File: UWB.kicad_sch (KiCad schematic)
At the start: 9 parts, among them U1 DWM3000TR13

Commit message: Final Routing
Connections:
- net +3.3V renamed +3.3V_Sensors
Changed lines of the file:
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@@
+	)
+	(junction
+		(at 177.8 90.17)
+		(diameter 0)
+		(color 0 0 0 0)
+	)
+	(junction
+		(at 111.76 87.63)
+		(diameter 0)
+		(color 0 0 0 0)
 	)
 	(junction
@@
 	)
 	(junction
-		(at 177.8 90.17)
-		(diameter 0)
-		(color 0 0 0 0)
-	)
-	(junction
-		(at 111.76 87.63)
-		(diameter 0)
-		(color 0 0 0 0)
-	)
-	(junction
 		(at 168.91 80.01)
 		(diameter 0)
@@
 		(pts
 			(xy 125.73 92.71) (xy 111.76 92.71)
+		)
+		(stroke
+			(width 0)
+			(type default)
+		)
+	)
+	(wire
+		(pts
+			(xy 101.6 78.74) (xy 101.6 87.63)
 		)
 		(stroke
@@
 			)
 			(justify right)
+		)
+	)
+	(hierarchical_label "+3.3V_Sensors"
+		(shape input)
+		(at 101.6 78.74 90)
+		(effects
+			(font
+				(size 1.27 1.27)
+			)
+			(justify left)
 		)
 	)
@@
 					(unit 1)
 				)
-			)
-		)
-	)
-	(symbol
-		(lib_id "power:+3.3V")
-		(at 101.6 87.63 0)
-		(unit 1)
-		(body_style 1)
-		(exclude_from_sim no)
-		(in_bom yes)
-		(on_board yes)
-		(in_pos_files yes)
-		(dnp no)
-		(fields_autoplaced yes)
-		(property "Reference" "#PWR02"
-			(at 101.6 91.44 0)
-			(hide yes)
-			(show_name no)
-			(do_not_autoplace no)
-			(effects
-				(font
-					(size 1.27 1.27)
-				)
-			)
-		)
-		(property "Value" "+3.3V"
-			(at 101.6 82.55 0)
-			(show_name no)
-			(do_not_autoplace no)
-			(effects
-				(font
-					(size 1.27 1.27)
-				)
-			)
-		)
-		(property "Footprint" "Package_SO:TSSOP-20_4.4x6.5mm_P0.65mm"
-			(at 101.6 87.63 0)
-			(hide yes)
-			(show_name no)
-			(do_not_autoplace no)
-			(effects
-				(font
-					(size 1.27 1.27)
-				)
-			)
-		)
-		(property "Datasheet" ""
-			(at 101.6 87.63 0)
-			(hide yes)
-			(show_name no)
-			(do_not_autoplace no)
-			(effects
-				(font
-					(size 1.27 1.27)
-				)
-			)
-		)
-		(property "Description" "Power symbol creates a global label with name \"+3.3V\""
-			(at 101.6 87.63 0)
-			(hide yes)
-			(show_name no)
-			(do_not_autoplace no)
-			(effects
-				(font
-					(size 1.27 1.27)
-				)
-			)
-		)
-		(pin "1"
-		)
-		(instances
-			(project "SuperNicePCB"
-				(path "/794e52b0-48ac-4476-a221-597be743d898/f7354725-387d-4beb-b227-ebab880fa3d1"
-					(reference "#PWR02")
-					(unit 1)
-				)

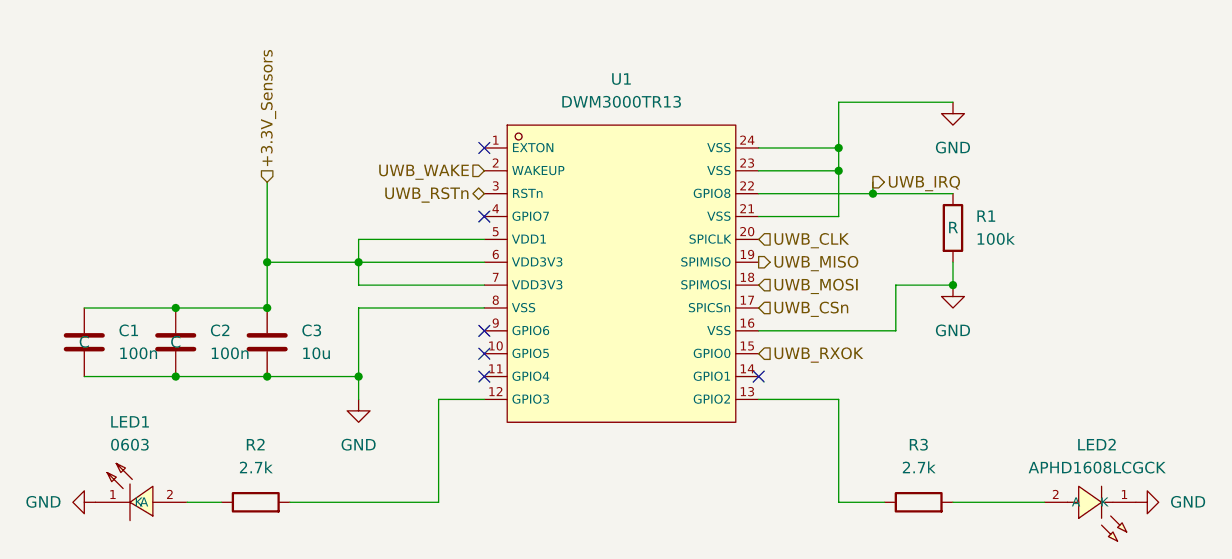
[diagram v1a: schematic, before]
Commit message: UWB: add test points
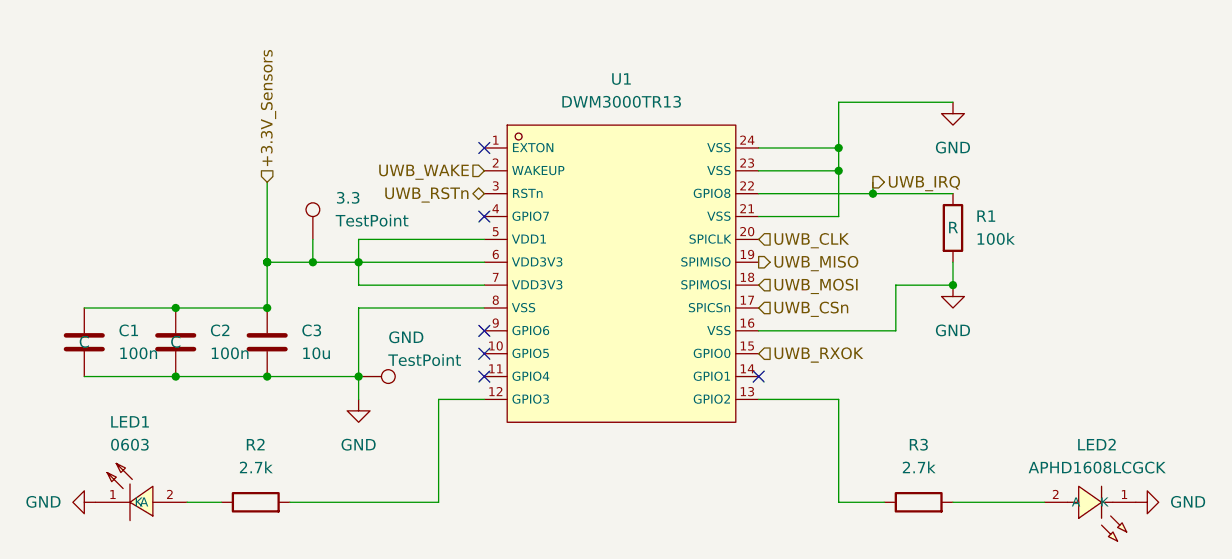
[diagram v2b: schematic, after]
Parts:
- added 3.3: TestPoint, Package_TO_SOT_SMD:SOT-23-5, symbol Connector:TestPoint
- added GND: TestPoint, symbol Connector:TestPoint
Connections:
- net +3.3V_Sensors: now also 3.3.1
- net GND: now also GND.1
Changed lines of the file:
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@@
+	)
+	(junction
+		(at 101.6 87.63)
+		(diameter 0)
+		(color 0 0 0 0)
+	)
+	(junction
+		(at 106.68 87.63)
+		(diameter 0)
+		(color 0 0 0 0)
 	)
 	(junction
@@
 	(wire
 		(pts
+			(xy 106.68 87.63) (xy 111.76 87.63)
+		)
+		(stroke
+			(width 0)
+			(type default)
+		)
+	)
+	(wire
+		(pts
 			(xy 165.1 77.47) (xy 165.1 82.55)
 		)
@@
 	(wire
 		(pts
-			(xy 101.6 87.63) (xy 111.76 87.63)
+			(xy 101.6 87.63) (xy 106.68 87.63)
 		)
 		(stroke
@@
 		(pts
 			(xy 171.45 95.25) (xy 171.45 90.17)
+		)
+		(stroke
+			(width 0)
+			(type default)
+		)
+	)
+	(wire
+		(pts
+			(xy 106.68 85.09) (xy 106.68 87.63)
 		)
 		(stroke
@@
 					(unit 1)
 				)
+			)
+		)
+	)
+	(symbol
+		(lib_id "Connector:TestPoint")
+		(at 111.76 100.33 270)
+		(unit 1)
+		(body_style 1)
+		(exclude_from_sim no)
+		(in_bom yes)
+		(on_board yes)
+		(in_pos_files yes)
+		(dnp no)
+		(property "Reference" "GND"
+			(at 115.062 96.012 90)
+			(show_name no)
+			(do_not_autoplace no)
+			(effects
+				(font
+					(size 1.27 1.27)
+				)
+				(justify left)
+			)
+		)
+		(property "Value" "TestPoint"
+			(at 115.062 98.552 90)
+			(show_name no)
+			(do_not_autoplace no)
+			(effects
+				(font
+					(size 1.27 1.27)
+				)
+				(justify left)
+			)
+		)
+		(property "Footprint" ""
+			(at 111.76 105.41 0)
+			(hide yes)
+			(show_name no)
+			(do_not_autoplace no)
+			(effects
+				(font
+					(size 1.27 1.27)
+				)
+			)
+		)
+		(property "Datasheet" ""
+			(at 111.76 105.41 0)
+			(hide yes)
+			(show_name no)
+			(do_not_autoplace no)
+			(effects
+				(font
+					(size 1.27 1.27)
+				)
+			)
+		)
+		(property "Description" "test point"
+			(at 111.76 100.33 0)
+			(hide yes)
+			(show_name no)
+			(do_not_autoplace no)
+			(effects
+				(font
+					(size 1.27 1.27)
+				)
+			)
+		)
+		(pin "1"
+		)
+		(instances
+			(project "SuperNicePCB"
+				(path "/794e52b0-48ac-4476-a221-597be743d898/f7354725-387d-4beb-b227-ebab880fa3d1"
+					(reference "GND")
+					(unit 1)
+				)
+			)
+		)
+	)
+	(symbol
+		(lib_id "Connector:TestPoint")
+		(at 106.68 85.09 0)
+		(unit 1)
+		(body_style 1)
+		(exclude_from_sim no)
+		(in_bom yes)
+		(on_board yes)
+		(in_pos_files yes)
+		(dnp no)
+		(fields_autoplaced yes)
+		(property "Reference" "3.3"
+			(at 109.22 80.5179 0)
+			(show_name no)
+			(do_not_autoplace no)
+			(effects
+				(font
+					(size 1.27 1.27)
+				)
+				(justify left)
+			)
+		)
+		(property "Value" "TestPoint"
+			(at 109.22 83.0579 0)
+			(show_name no)
+			(do_not_autoplace no)
+			(effects
+				(font
+					(size 1.27 1.27)
+				)
+				(justify left)
+			)
+		)
+		(property "Footprint" "Package_TO_SOT_SMD:SOT-23-5"
+			(at 111.76 85.09 0)
+			(hide yes)
+			(show_name no)
+			(do_not_autoplace no)
+			(effects
+				(font
+					(size 1.27 1.27)
+				)
+			)
+		)
+		(property "Datasheet" ""
+			(at 111.76 85.09 0)
+			(hide yes)
+			(show_name no)
+			(do_not_autoplace no)
+			(effects
+				(font
+					(size 1.27 1.27)
+				)
+			)
+		)
+		(property "Description" "test point"
+			(at 106.68 85.09 0)
+			(hide yes)
+			(show_name no)
+			(do_not_autoplace no)
+			(effects
+				(font
+					(size 1.27 1.27)
+				)
+			)
+		)
+		(pin "1"
+		)
+		(instances
+			(project "SuperNicePCB"
+				(path "/794e52b0-48ac-4476-a221-597be743d898/f7354725-387d-4beb-b227-ebab880fa3d1"
+					(reference "3.3")
+					(unit 1)
+				)

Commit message: refactor: reposition GPIO debug connector and update schematic wiring
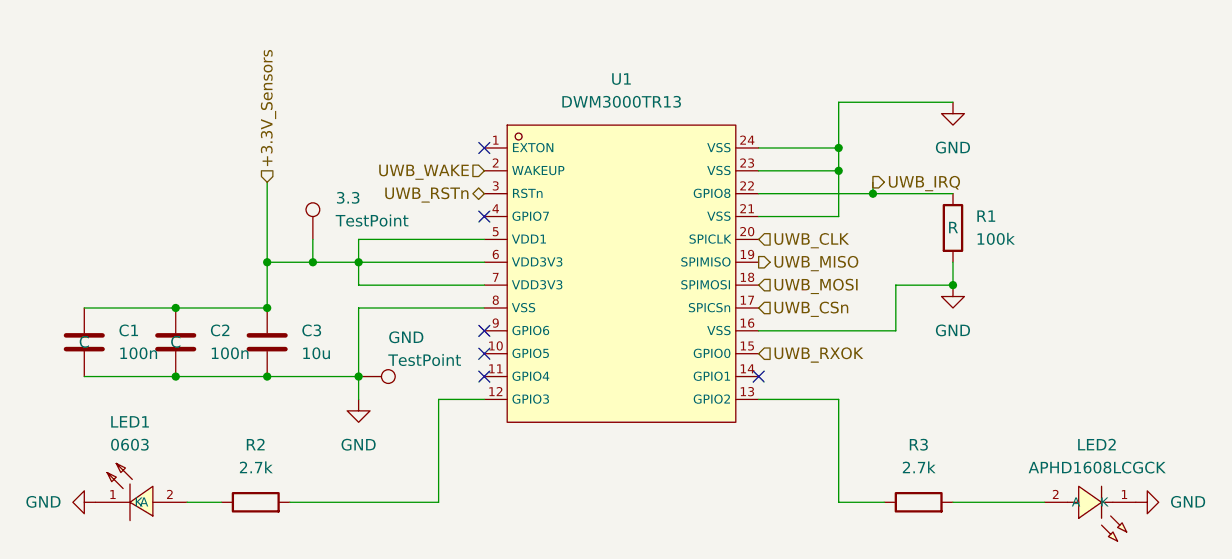
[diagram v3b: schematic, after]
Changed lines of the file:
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@@
-	)
-	(junction
-		(at 101.6 87.63)
-		(diameter 0)
-		(color 0 0 0 0)
 	)
 	(junction

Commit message: Annotate whole schematic with per-sheet numbering (x100)
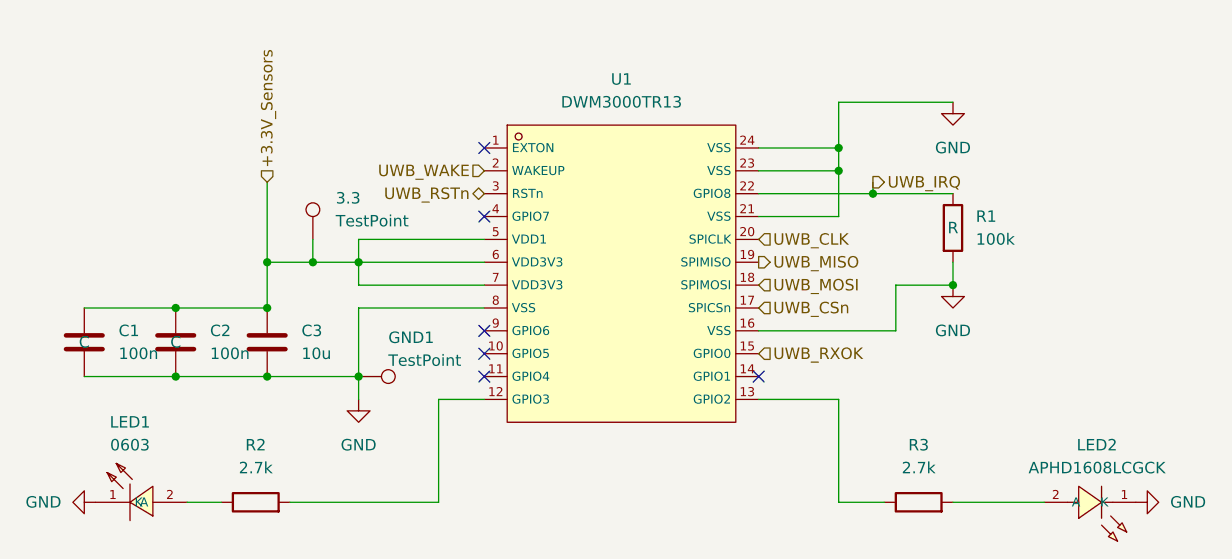
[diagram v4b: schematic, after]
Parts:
- renumbered GND to GND1
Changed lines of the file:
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@@
 		(in_pos_files yes)
 		(dnp no)
-		(property "Reference" "GND"
+		(property "Reference" "GND1"
 			(at 115.062 96.012 90)
 			(show_name no)
@@
 			(project "SuperNicePCB"
 				(path "/794e52b0-48ac-4476-a221-597be743d898/f7354725-387d-4beb-b227-ebab880fa3d1"
-					(reference "GND")
+					(reference "GND1")
 					(unit 1)
 				)

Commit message: Changed the default symbols with JLC's one
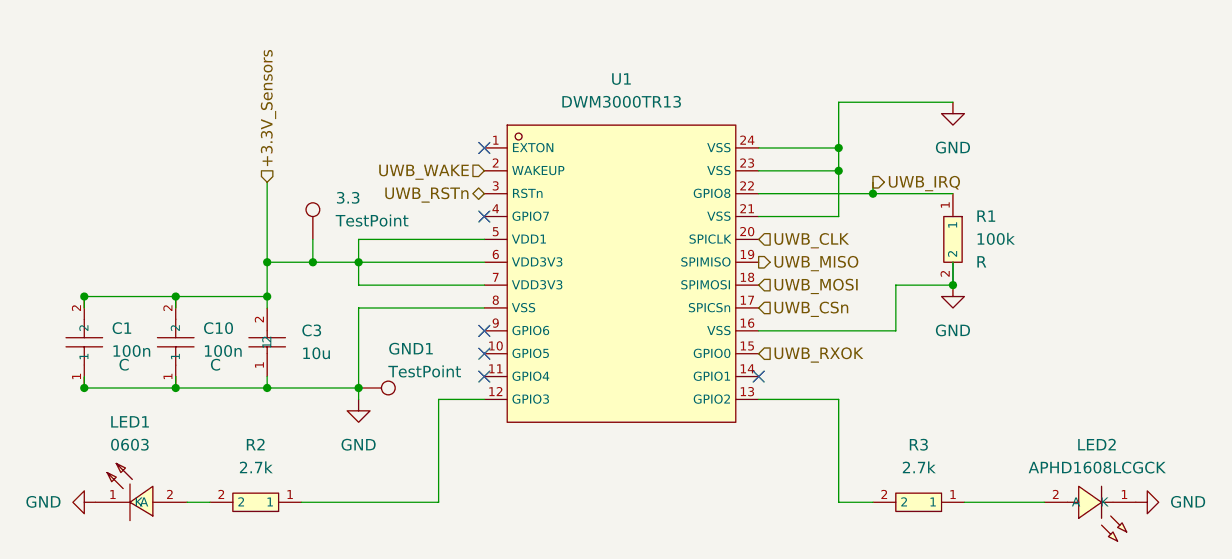
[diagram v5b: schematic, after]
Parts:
- removed C2: 100n, symbol Device:C
- added C10: 100n, lcsc_footprints:C1525_C0402, symbol lcsc_imported:100nF_(104)_±10%_16V
- C1: footprint (none) -> lcsc_footprints:C1525_C0402; symbol Device:C -> lcsc_imported:100nF_(104)_±10%_16V; LCSC (none) -> C1525; Manufacturer (none) -> SAMSUNG(三星)
- C3: footprint (none) -> lcsc_footprints:C1713_C0805; symbol Device:C -> lcsc_imported:10uF_(106)_±10%_16V; LCSC (none) -> C1713; Manufacturer (none) -> SAMSUNG(三星)
- R1: footprint lcsc_footprints:C5299931_WIRELM-SMD_DWM3000TR13 -> lcsc_footprints:C14675_R0603; symbol Device:R -> lcsc_imported:RC0603FR-07100KL; LCSC (none) -> C14675; Manufacturer (none) -> YAGEO(国巨)
- R2, R3: footprint lcsc_footprints:C5139863_LED-SMD_L1_6-W0_8-RD_GREEN-1 -> lcsc_footprints:C13167_R0603; symbol Device:R -> lcsc_imported:2_7KΩ_(2701)_±1%; LCSC (none) -> C13167; Manufacturer (none) -> UNI-ROYAL(厚声)
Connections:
- net +3.3V_Sensors: now also C1.2, C3.2, C10.2; no longer C1.1, C3.1
- net GND: now also C1.1, C3.1, C10.1; no longer C1.2, C3.2
- net at U1.12 (GPIO3): now also R2.1; no longer R2.2
- net at U1.13 (GPIO2): now also R3.2; no longer R3.1
- net at LED1.2 (A): now also R2.2; no longer R2.1
- net at LED2.2 (A): now also R3.1; no longer R3.2
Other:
- moved on the sheet: GND1

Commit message: Changed footprint of the test point
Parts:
- 3.3: footprint Package_TO_SOT_SMD:SOT-23-5 -> TestPoint:TestPoint_Pad_1.0x1.0mm
- GND1: footprint (none) -> TestPoint:TestPoint_Pad_1.0x1.0mm
- renumbered C1 to C18, C10 to C19, C3 to C20, R2 to R16, R3 to R17, R1 to R18, U1 to U9
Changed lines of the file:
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@@
 		(dnp no)
 		(fields_autoplaced yes)
-		(property "Reference" "#PWR06"
+		(property "Reference" "#PWR014"
 			(at 76.2 114.3 0)
 			(hide yes)
@@
 			(project "SuperNicePCB"
 				(path "/794e52b0-48ac-4476-a221-597be743d898/f7354725-387d-4beb-b227-ebab880fa3d1"
-					(reference "#PWR06")
+					(reference "#PWR014")
 					(unit 1)
 				)
@@
 		(dnp no)
 		(fields_autoplaced yes)
-		(property "Reference" "U1"
+		(property "Reference" "U9"
 			(at 140.97 67.31 0)
 			(show_name no)
@@
 			(project "SuperNicePCB"
 				(path "/794e52b0-48ac-4476-a221-597be743d898/f7354725-387d-4beb-b227-ebab880fa3d1"
-					(reference "U1")
+					(reference "U9")
 					(unit 1)
 				)
@@
 		(dnp no)
 		(fields_autoplaced yes)
-		(property "Reference" "R2"
+		(property "Reference" "R16"
 			(at 100.33 107.95 0)
 			(show_name no)
@@
 			(project "SuperNicePCB"
 				(path "/794e52b0-48ac-4476-a221-597be743d898/f7354725-387d-4beb-b227-ebab880fa3d1"
-					(reference "R2")
+					(reference "R16")
 					(unit 1)
 				)
@@
 		(dnp no)
 		(fields_autoplaced yes)
-		(property "Reference" "#PWR05"
+		(property "Reference" "#PWR018"
 			(at 204.47 114.3 0)
 			(hide yes)
@@
 			(project "SuperNicePCB"
 				(path "/794e52b0-48ac-4476-a221-597be743d898/f7354725-387d-4beb-b227-ebab880fa3d1"
-					(reference "#PWR05")
+					(reference "#PWR018")
 					(unit 1)
 				)
@@
 		(in_pos_files yes)
 		(dnp no)
-		(property "Reference" "C1"
+		(property "Reference" "C18"
 			(at 84.328 94.996 90)
 			(show_name no)
@@
 			(project "SuperNicePCB"
 				(path "/794e52b0-48ac-4476-a221-597be743d898/f7354725-387d-4beb-b227-ebab880fa3d1"
-					(reference "C1")
+					(reference "C18")
 					(unit 1)
 				)
@@
 			)
 		)
-		(property "Footprint" ""
+		(property "Footprint" "TestPoint:TestPoint_Pad_1.0x1.0mm"
 			(at 111.76 106.68 0)
 			(hide yes)
@@
 			)
 		)
-		(property "Footprint" "Package_TO_SOT_SMD:SOT-23-5"
+		(property "Footprint" "TestPoint:TestPoint_Pad_1.0x1.0mm"
 			(at 111.76 85.09 0)
 			(hide yes)
@@
 		(dnp no)
 		(fields_autoplaced yes)
-		(property "Reference" "#PWR04"
+		(property "Reference" "#PWR016"
 			(at 177.8 76.2 0)
 			(hide yes)
@@
 			(project "SuperNicePCB"
 				(path "/794e52b0-48ac-4476-a221-597be743d898/f7354725-387d-4beb-b227-ebab880fa3d1"
-					(reference "#PWR04")
+					(reference "#PWR016")
 					(unit 1)
 				)
@@
 		(in_pos_files yes)
 		(dnp no)
-		(property "Reference" "C10"
+		(property "Reference" "C19"
 			(at 94.488 94.996 90)
 			(show_name no)
@@
 			(project "SuperNicePCB"
 				(path "/794e52b0-48ac-4476-a221-597be743d898/f7354725-387d-4beb-b227-ebab880fa3d1"
-					(reference "C10")
+					(reference "C19")
 					(unit 1)
 				)
@@
 		(dnp no)
 		(fields_autoplaced yes)
-		(property "Reference" "#PWR03"
+		(property "Reference" "#PWR015"
 			(at 111.76 109.22 0)
 			(hide yes)
@@
 			(project "SuperNicePCB"
 				(path "/794e52b0-48ac-4476-a221-597be743d898/f7354725-387d-4beb-b227-ebab880fa3d1"
-					(reference "#PWR03")
+					(reference "#PWR015")
 					(unit 1)
 				)
@@
 		(dnp no)
 		(fields_autoplaced yes)
-		(property "Reference" "R3"
+		(property "Reference" "R17"
 			(at 173.99 107.95 0)
 			(show_name no)
@@
 			(project "SuperNicePCB"
 				(path "/794e52b0-48ac-4476-a221-597be743d898/f7354725-387d-4beb-b227-ebab880fa3d1"
-					(reference "R3")
+					(reference "R17")
 					(unit 1)
 				)
@@
 		(dnp no)
 		(fields_autoplaced yes)
-		(property "Reference" "C3"
+		(property "Reference" "C20"
 			(at 105.41 95.2499 90)
 			(show_name no)
@@
 			(project "SuperNicePCB"
 				(path "/794e52b0-48ac-4476-a221-597be743d898/f7354725-387d-4beb-b227-ebab880fa3d1"
-					(reference "C3")
+					(reference "C20")
 					(unit 1)
 				)
@@
 		(dnp no)
 		(fields_autoplaced yes)
-		(property "Reference" "R1"
+		(property "Reference" "R18"
 			(at 180.34 82.5499 90)
 			(show_name no)
@@
 			(project "SuperNicePCB"
 				(path "/794e52b0-48ac-4476-a221-597be743d898/f7354725-387d-4beb-b227-ebab880fa3d1"
-					(reference "R1")
+					(reference "R18")
 					(unit 1)
 				)
@@
 		(dnp no)
 		(fields_autoplaced yes)
-		(property "Reference" "#PWR01"
+		(property "Reference" "#PWR017"
 			(at 177.8 96.52 0)
 			(hide yes)
@@
 			(project "SuperNicePCB"
 				(path "/794e52b0-48ac-4476-a221-597be743d898/f7354725-387d-4beb-b227-ebab880fa3d1"
-					(reference "#PWR01")
+					(reference "#PWR017")
 					(unit 1)
 				)

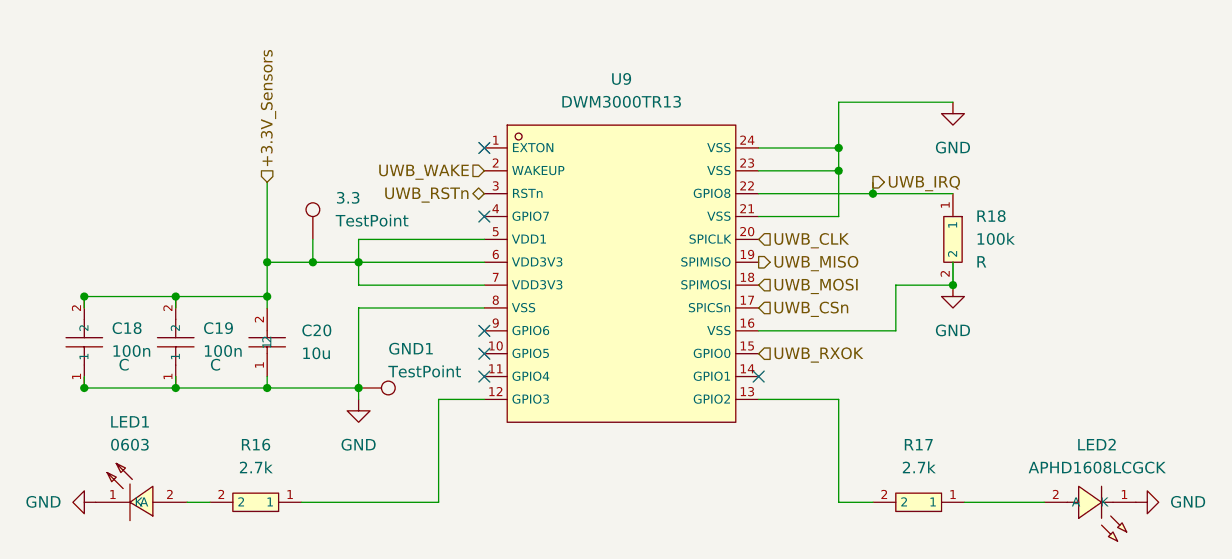
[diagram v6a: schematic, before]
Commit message: placement rework of sensors and uwb, installation of power plane, starting of routing , UWB sheet net names aligned with MCU
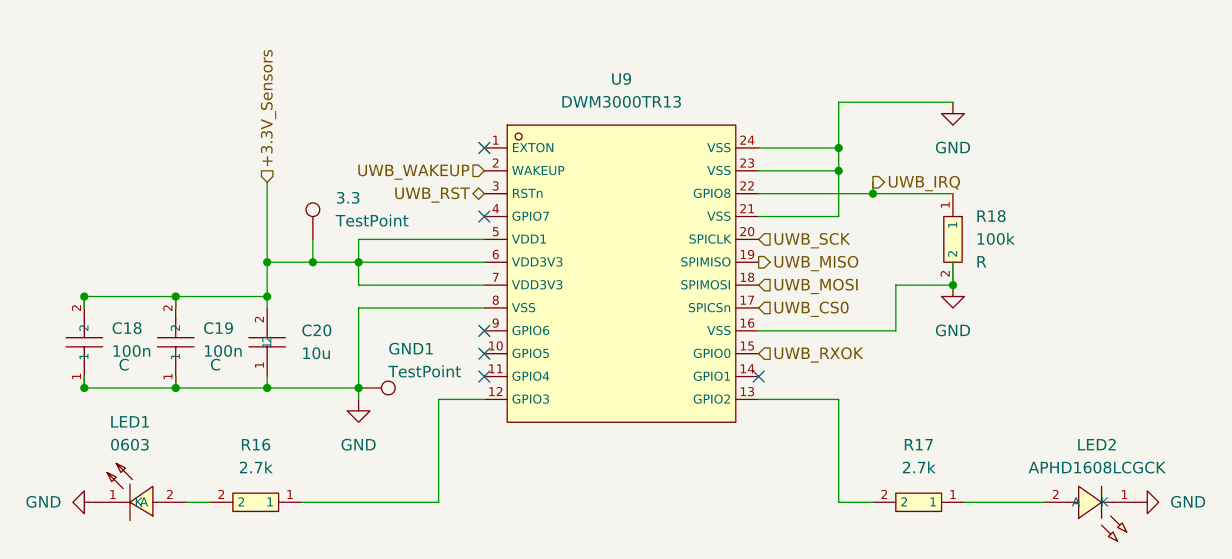
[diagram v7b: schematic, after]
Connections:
- net UWB_CLK renamed UWB_SCK
- net UWB_CSn renamed UWB_CS0
- net UWB_RSTn renamed UWB_RST
- net UWB_WAKE renamed UWB_WAKEUP
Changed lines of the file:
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@@
 		)
 	)
-	(hierarchical_label "UWB_WAKE"
+	(hierarchical_label "UWB_WAKEUP"
 		(shape input)
 		(at 125.73 77.47 180)
@@
 		)
 	)
-	(hierarchical_label "UWB_RSTn"
+	(hierarchical_label "UWB_RST"
 		(shape bidirectional)
 		(at 125.73 80.01 180)
@@
 		)
 	)
-	(hierarchical_label "UWB_CLK"
+	(hierarchical_label "UWB_SCK"
 		(shape input)
 		(at 156.21 85.09 0)
@@
 		)
 	)
-	(hierarchical_label "UWB_CSn"
+	(hierarchical_label "UWB_CS0"
 		(shape input)
 		(at 156.21 92.71 0)
